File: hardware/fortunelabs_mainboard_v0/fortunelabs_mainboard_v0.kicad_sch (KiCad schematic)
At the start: 32 parts, among them J1 Conn_02x16_Odd_Even, J2 Conn_02x16_Odd_Even, U1 ADS1115, U2 MCP23017_ML, U3 ESP32-S3-WROOM-2, U4 ADS1115

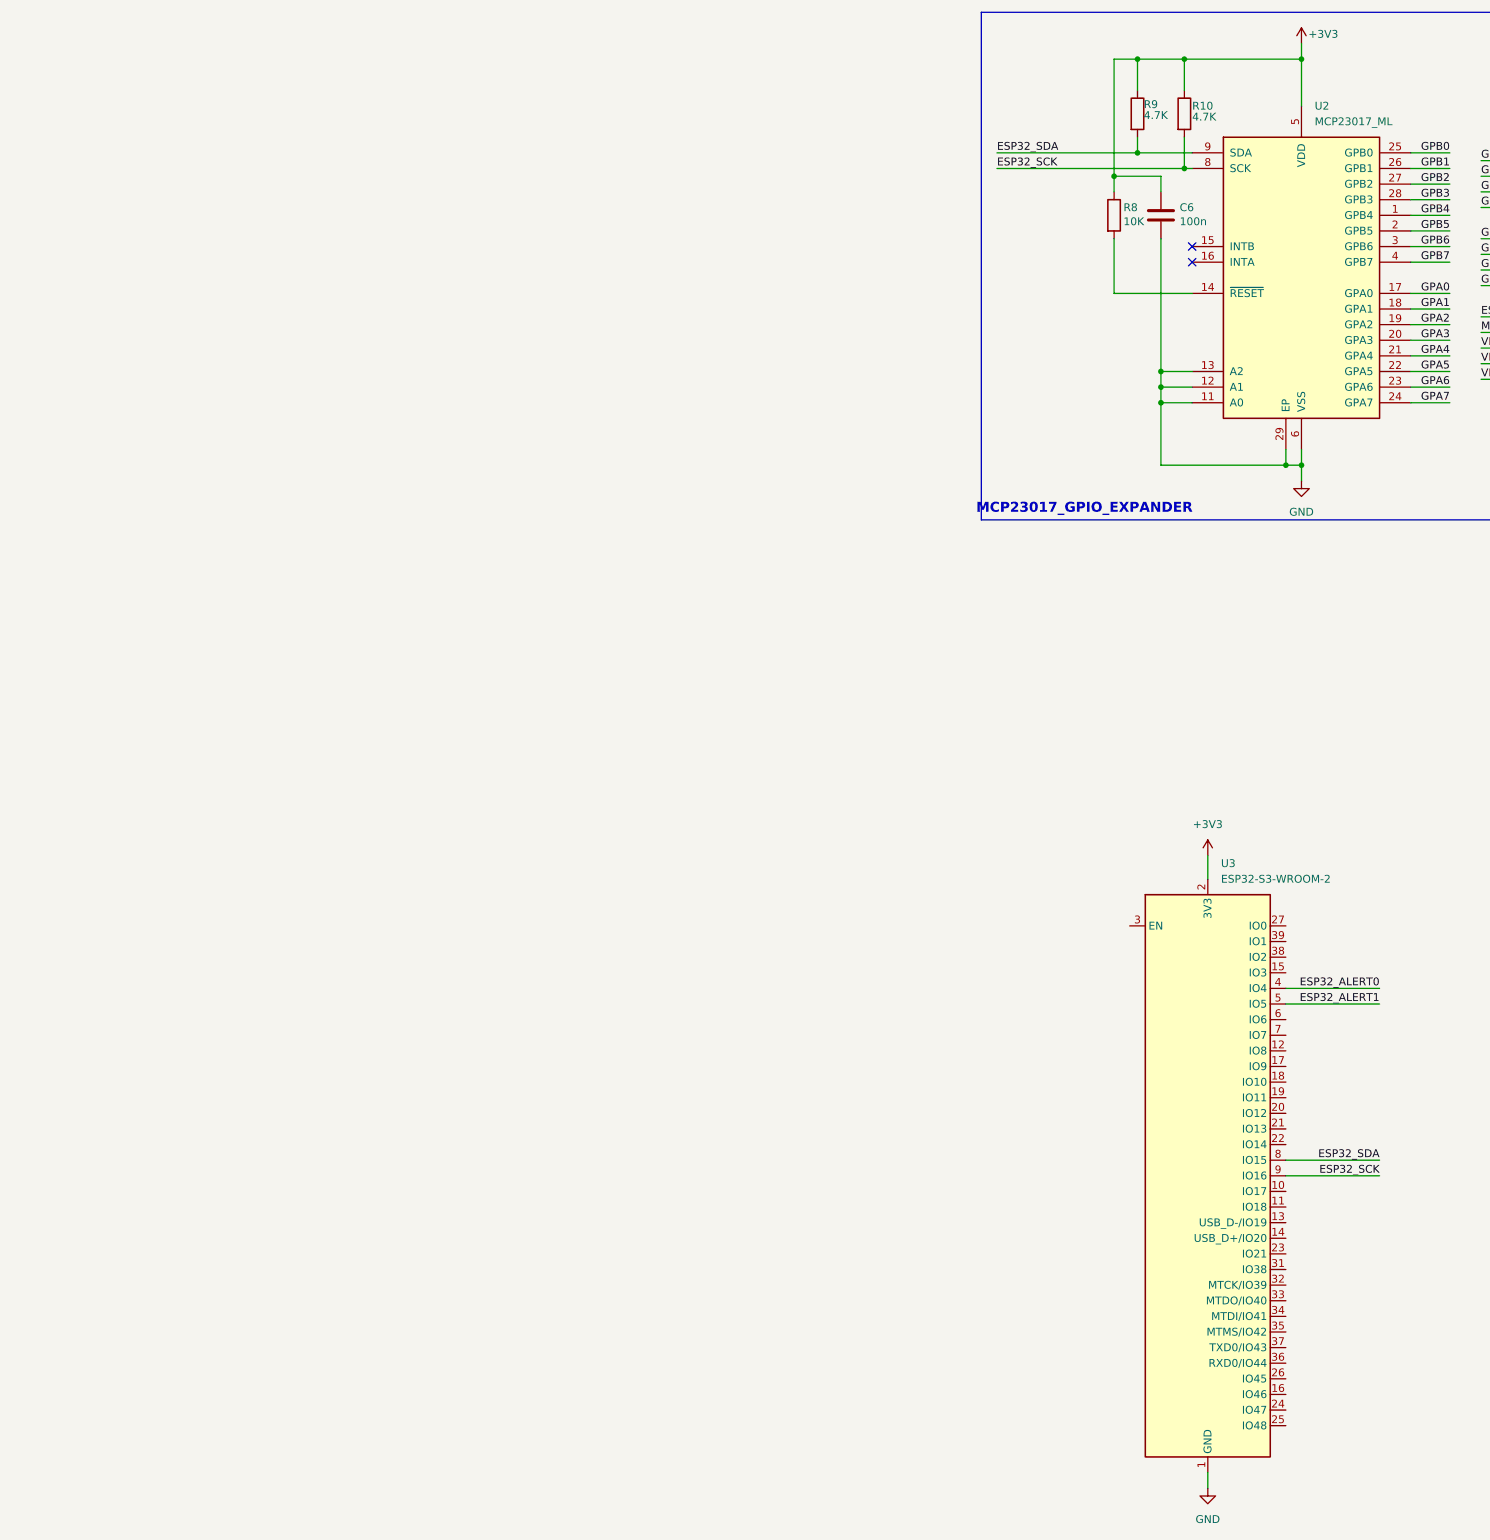
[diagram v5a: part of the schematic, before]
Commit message: feat: adding power management module
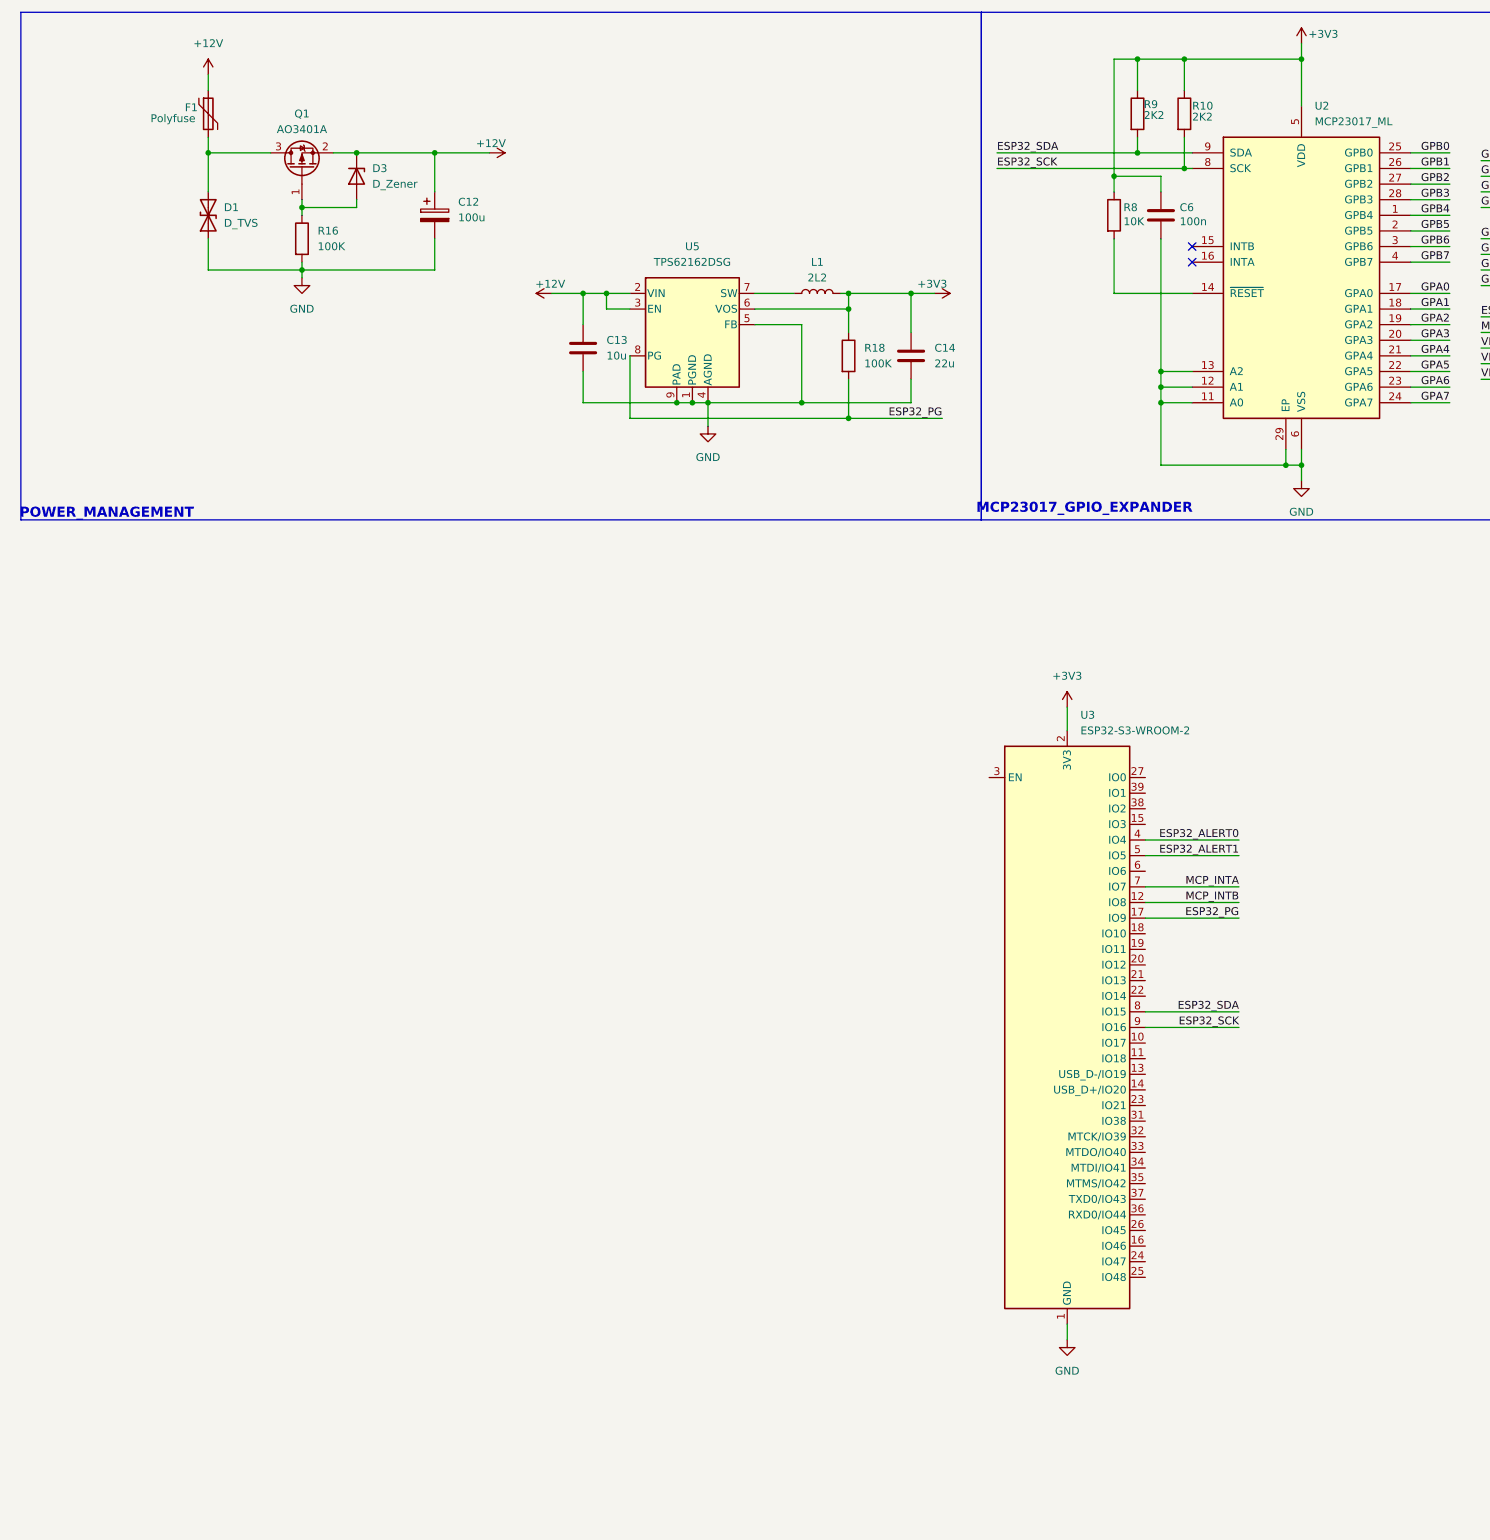
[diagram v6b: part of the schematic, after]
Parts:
- added C12: 100u, symbol Device:C_Polarized
- added C13: 10u, symbol Device:C
- added C14: 22u, symbol Device:C
- added D1: D_TVS, symbol Device:D_TVS
- added D3: D_Zener, symbol Device:D_Zener
- added F1: Polyfuse, symbol Device:Polyfuse
- added L1: 2L2, symbol Device:L
- added Q1: AO3401A, Package_TO_SOT_SMD:SOT-23, symbol Transistor_FET:AO3401A
- added R16, R18: 100K, symbol Device:R
- added U5: TPS62162DSG, Package_SON:WSON-8-1EP_2x2mm_P0.5mm_EP0.9x1.6mm_ThermalVias, symbol Regulator_Switching:TPS62162DSG
- R10, R9: value 4.7K -> 2K2
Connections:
- net +3V3: now also C14.2, L1.2, R18.1, U5.6 (VOS)
- net GND: now also C12.2, C13.2, C14.1, D1.1 (A1), R16.2, U5.1 (PGND), U5.4 (AGND), U5.5 (FB), U5.9 (PAD)
- net MCP_INTA: now also U3.7 (IO7)
- net MCP_INTB: now also U3.12 (IO8)
- net ESP32_PG: now reaches U3.17 (IO9)
- net ESP32_PG: now also R18.2, U5.8 (PG)
- new net: D3.2 (A), Q1.1 (G), R16.1
- new net: D1.2 (A2), F1.2, Q1.3 (D)
- new net: L1.1, U5.7 (SW)
- new net +12V: C12.1, C13.1, D3.1 (K), F1.1, Q1.2 (S), U5.2 (VIN), U5.3 (EN)
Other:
- note added: "POWER_MANAGEMENT"
- moved on the sheet: U3

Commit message: feat: adding usb c module
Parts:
- added C15: 100n, symbol Device:C
- added C16: 100u, symbol Device:C
- added C17: C, symbol Device:C
- added J3: USB_C_Receptacle_USB2.0_14P, symbol Connector:USB_C_Receptacle_USB2.0_14P
- added J4: SD_Card_Receptacle, symbol Connector:SD_Card_Receptacle
- added R18, R19: 5K1, symbol Device:R
- added RN1: R_Network05, Resistor_THT:R_Array_SIP6, symbol Device:R_Network05
- added U6: DS3232M, Package_SO:SOIC-8_3.9x4.9mm_P1.27mm, symbol Timer_RTC:DS3232M
- renumbered R18 to R17
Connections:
- net +3V3: now also C15.1, C16.1, C17.1, J4.4 (VDD), RN1.1 (common), U6.2 (VCC)
- net GND: now also C15.2, C16.2, C17.2, J3.A1 (GND), J3.A12 (GND), J3.B1 (GND), J3.B12 (GND), J3.S1 (SHIELD), J4.12 (SHELL1), J4.13 (SHELL2), J4.3 (VSS), J4.6 (VSS), R18.2, R19.2, U6.5 (GND)
- net USB_D-: now reaches U3.13 (USB_D-/IO19)
- net USB_D-: now also J3.A7 (D-), J3.B7 (D-)
- net USB_D+: now reaches U3.14 (USB_D+/IO20)
- net USB_D+: now also J3.A6 (D+), J3.B6 (D+)
- net SD_CS: now reaches U3.18 (IO10)
- net SD_CS: now also J4.1 (CD/DAT3), RN1.3 (R2)
- net SD_MOSI: now reaches U3.19 (IO11)
- net SD_MOSI: now also J4.2 (CMD), RN1.2 (R1)
- net SD_CLK: now reaches U3.20 (IO12)
- net SD_CLK: now also J4.5 (CLK)
- net SD_MISO: now reaches U3.21 (IO13)
- net SD_MISO: now also J4.7 (DAT0), RN1.6 (R5)
- new net: J3.A4 (VBUS), J3.A9 (VBUS), J3.B4 (VBUS), J3.B9 (VBUS)
- new net: J3.A5 (CC1), R19.1
- new net: J3.B5 (CC2), R18.1
- new net: J4.9 (DAT2), RN1.4 (R3)
- new net: J4.8 (DAT1), RN1.5 (R4)
- no-connect marks 7 -> 10
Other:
- note added: "RTC"
- note added: "SPI_SD_CARD"
- note added: "USB_C_INTERFACE"
- moved on the sheet: C12, C13, C14, D1, D3, F1, L1, Q1, R16, R17, U3, U5

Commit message: feat: finshing schematic for v0.2
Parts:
- added BT1: Battery_Cell, CR2032, symbol Device:Battery_Cell
- added C18: C, symbol Device:C
- added D10: LED, LED_SMD:LED_0805_2012Metric, symbol Device:LED
- added D2, D4, D5, D6, D7, D8, D9: LED, symbol Device:LED
- added J5: Conn_02x07_Odd_Even, symbol Connector_Generic:Conn_02x07_Odd_Even
- added R20, R24: 10K, symbol Device:R
- added R21, R23: R, symbol Device:R
- added R22: 14K3, symbol Device:R
- added R25, R26, R27, R28, R29, R30, R31, R32: DNP, symbol Device:R
- added R33, R34, R35, R36, R37, R38, R39, R40: 470, symbol Device:R
- added SW1: BOOT, symbol Switch:SW_Push
- added SW2: RESET, symbol Switch:SW_Push
- added U7: TPL5010, Package_TO_SOT_SMD:SOT-23-6, symbol Timer:TPL5010
- added U8: ULN2803A, symbol Transistor_Array:ULN2803A
- C17: value C -> 100n
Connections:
- net +12V: now also J5.13 (Pin_13), J5.14 (Pin_14)
- net +3V3: now also U3.10 (IO17), J5.1 (Pin_1), J5.2 (Pin_2), J5.3 (Pin_3), J5.4 (Pin_4), J5.5 (Pin_5), J5.6 (Pin_6), J5.7 (Pin_7), J5.8 (Pin_8), R20.2, R21.1, R23.1, R24.2, R33.1, R34.1, R35.1, R36.1, R37.1, R38.1, R39.1, R40.1, SW1.1, SW2.2, U7.1 (VDD), U8.11 (O8), U8.12 (O7), U8.13 (O6), U8.14 (O5), U8.15 (O4), U8.16 (O3), U8.17 (O2), U8.18 (O1)
- net ESP32_SCK: now also U6.8 (SCL)
- net ESP32_SDA: now also U6.7 (SDA)
- net GND: now also BT1.2 (-), C18.2, D10.1 (K), D2.1 (K), D4.1 (K), D5.1 (K), D6.1 (K), D7.1 (K), D8.1 (K), D9.1 (K), J5.11 (Pin_11), J5.12 (Pin_12), R22.2, SW1.2, SW2.1, U7.2 (GND), U8.9 (GND)
- net GPB0: now also R25.1
- net GPB1: now also R26.1
- net GPB2: now also R27.1
- net GPB3: now also R28.1
- net GPB4: now also R29.1
- net GPB5: now also R30.1
- net GPB6: now also R31.1
- net GPB7: now also R32.1
- net at U3.27 (IO0): now also R24.1
- net ESP32_EN: now reaches U3.3 (EN)
- net ESP32_EN: now also C18.1, R21.2, R23.2, U7.6 (~{RST})
- net ESP32_WDT_DONE: now reaches U3.6 (IO6)
- net ESP32_WDT_DONE: now also U7.4 (DONE)
- net at U6.3 (~{INT}/SQW): now also R20.1
- net at U6.6 (VBAT): now also BT1.1 (+)
- new net: D4.2 (A), R34.2
- new net: D2.2 (A), R33.2
- new net: R32.2, U8.8 (I8)
- new net: D6.2 (A), R36.2
- new net: D10.2 (A), R40.2
- new net: R30.2, U8.6 (I6)
- new net: R28.2, U8.4 (I4)
- new net: D5.2 (A), R35.2
- new net: D7.2 (A), R37.2
- new net: R25.2, U8.1 (I1)
- new net: R26.2, U8.2 (I2)
- new net: R27.2, U8.3 (I3)
- new net: R29.2, U8.5 (I5)
- new net: R31.2, U8.7 (I7)
- new net: R22.1, U7.3 (DELAY/M_RST)
- new net: D8.2 (A), R38.2
- new net: D9.2 (A), R39.2
- new net COM: J5.10 (Pin_10), J5.9 (Pin_9), U8.10 (COM)
- no-connect marks 10 -> 13
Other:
- note added: "ESP_32_S3_WROOM2"
- note added: "OUTPUT_DRIVER_ARRAY"
- note added: "R25-R32 DNP"
- note added: "R33-R40 470"
- note added: "REALTIME_CLOCK"
- note added: "WATCHDOG"
- note removed: "RTC"
- moved on the sheet: C12, C17, D1, D3, F1, Q1, R16, U3, U6
